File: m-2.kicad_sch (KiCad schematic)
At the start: 12 parts

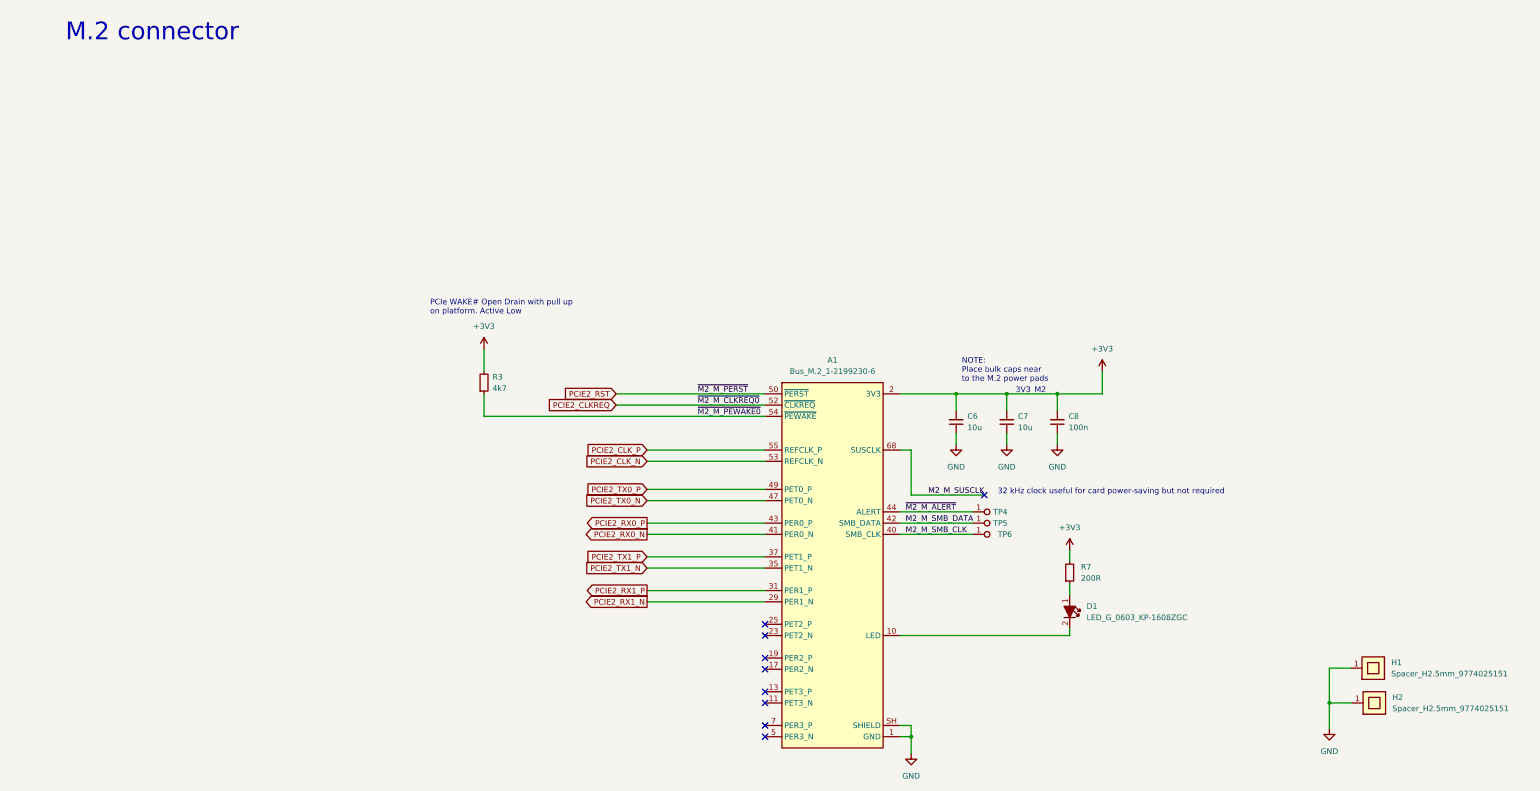
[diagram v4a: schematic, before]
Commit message: [#45990] Fix schematic flaws discussed in review
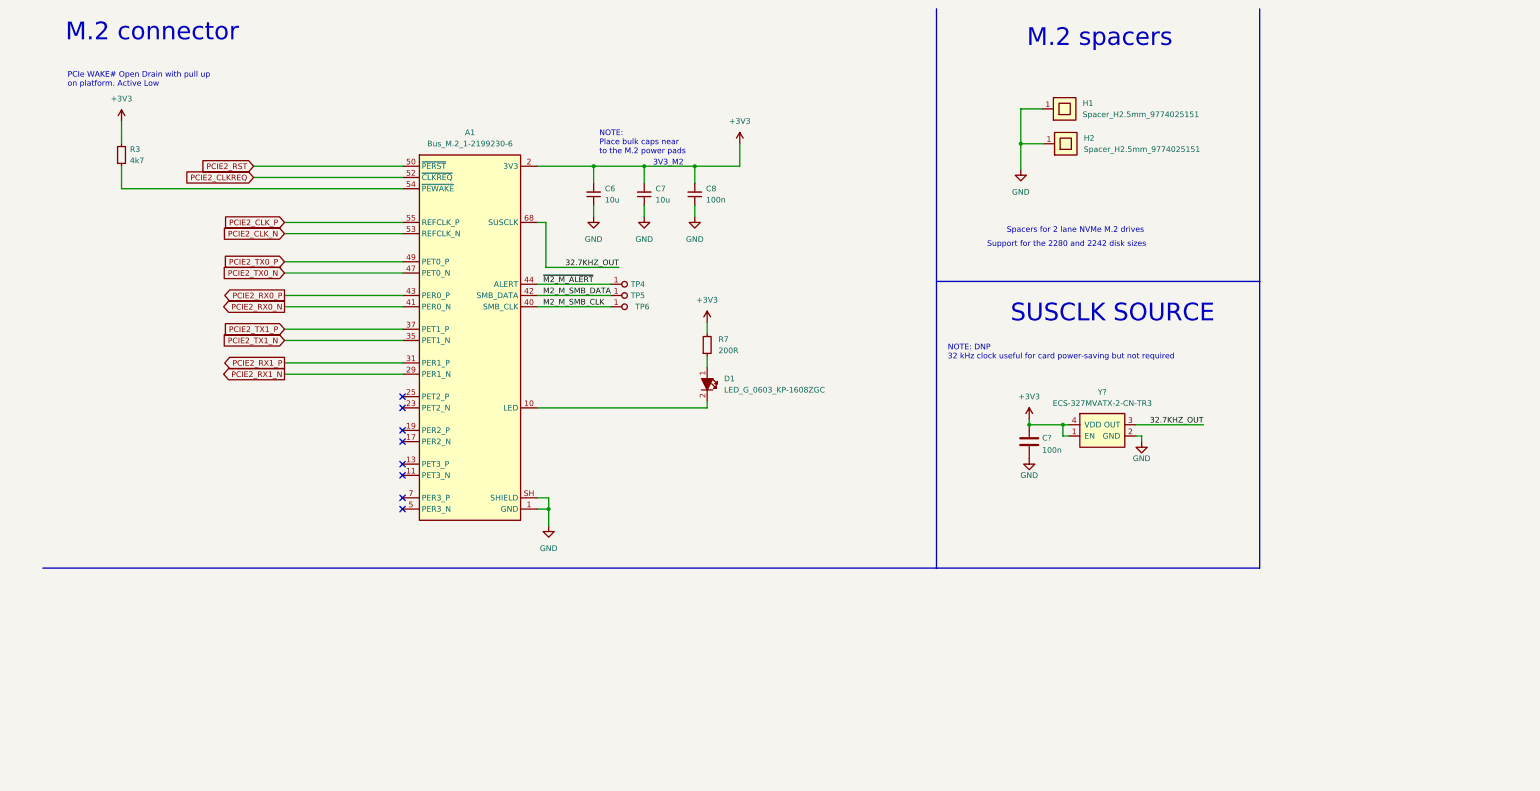
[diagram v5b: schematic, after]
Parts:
- added C?: C_100n_0402, jetson-orin-baseboard-footprints:0402-cap, symbol jetson-orin-baseboard:C_100n_0402
- added Y?: ECS-327MVATX-2-CN-TR3, jetson-orin-baseboard-footprints:Oscillator_SMD_ECS_2520MV-xxx-xx-4Pin_2.5x2.0mm, symbol jetson-orin-baseboard:ECS-327MVATX-2-CN-TR3
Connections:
- net +3V3: now also C?.1, Y?.1 (EN), Y?.4 (VDD)
- net GND: now also C?.2, Y?.2 (GND)
- net M2_M_SUSCLK renamed 32.7KHZ_OUT
- net 32.7KHZ_OUT: now also Y?.3 (OUT)
- net ~{M2_M_PEWAKE0}: no longer names the net of A1.54 (~{PEWAKE}), R3.1
- no-connect marks 9 -> 8
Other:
- note added: "M.2 spacers"
- note added: "NOTE: DNP 32 kHz clock useful for card power-saving but not required"
- note added: "SUSCLK SOURCE"
- note added: "Spacers for 2 lane NVMe M.2 drives"
- note added: "Support for the 2280 and 2242 disk sizes"
- note removed: "32 kHz clock useful for card power-saving but not required"
- moved on the sheet: A1, C6, C7, C8, D1, H1, H2, R3, R7, TP4, TP5, TP6

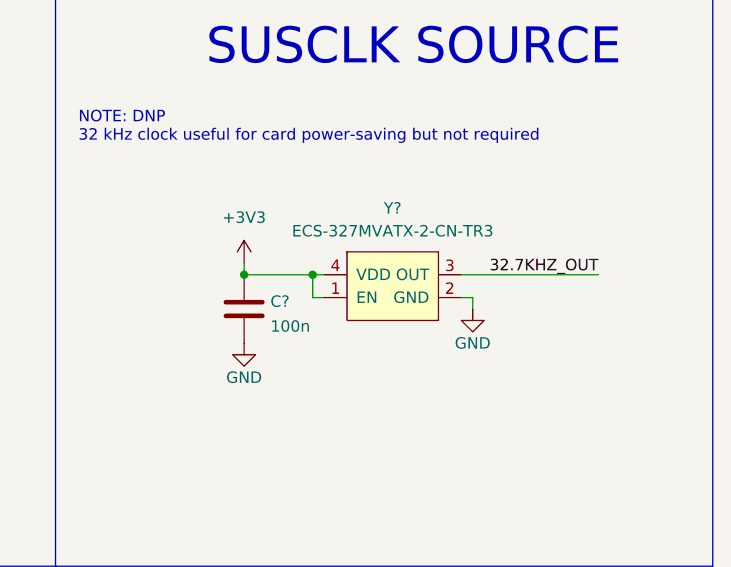
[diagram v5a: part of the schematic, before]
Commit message: [#45990] Route dif Pcie, place susclk gen
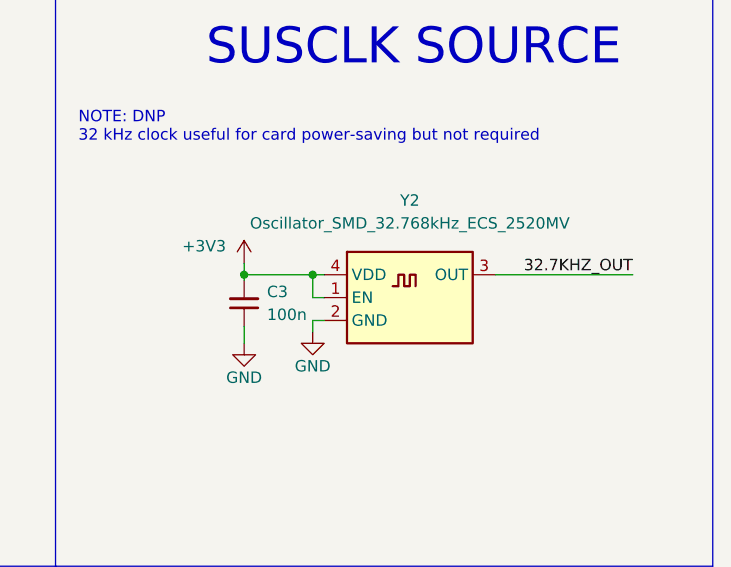
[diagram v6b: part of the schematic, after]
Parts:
- removed C?: C_100n_0402, jetson-orin-baseboard-footprints:0402-cap, symbol jetson-orin-baseboard:C_100n_0402
- removed Y?: ECS-327MVATX-2-CN-TR3, jetson-orin-baseboard-footprints:Oscillator_SMD_ECS_2520MV-xxx-xx-4Pin_2.5x2.0mm, symbol jetson-orin-baseboard:ECS-327MVATX-2-CN-TR3
- added C3: C_100n_0402, antmicro-footprints:C_0402_1005Metric, symbol antmicroCapacitors0402:C_100n_0402
- added Y2: Oscillator_SMD_32.768kHz_ECS_2520MV, antmicro-footprints:Oscillator_SMD_ECS_2520MV_2.5x2mm, symbol antmicroOscillators:Oscillator_SMD_32.768kHz_ECS_2520MV
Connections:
- net +3V3: now also C3.2, Y2.1 (EN), Y2.4 (VDD)
- net 32.7KHZ_OUT: now also Y2.3 (OUT)
- net GND: now also C3.1, Y2.2 (GND)
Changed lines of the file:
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@@
   (no_connect (at 93.345 117.475))
   (no_connect (at 93.345 125.095))
-  (wire (pts (xy 259.08 108.585) (xy 260.35 108.585))
+  (wire (pts (xy 243.84 111.125) (xy 242.57 111.125))
     (stroke (width 0) (type default) (color 0 0 0 0))
   )
@@
     (stroke (width 0) (type default) (color 0 0 0 0))
   )
+  (wire (pts (xy 234.95 111.76) (xy 234.95 113.665))
+    (stroke (width 0) (type default) (color 0 0 0 0))
+  )
   (polyline (pts (xy 287.02 12.065) (xy 287.02 73.66))
     (stroke (width 0) (type default) (color 0 0 0 0))
@@
     (stroke (width 0) (type default) (color 0 0 0 0))
   )
-  (wire (pts (xy 260.35 108.585) (xy 260.35 109.855))
+  (wire (pts (xy 242.57 111.125) (xy 242.57 112.395))
     (stroke (width 0) (type default) (color 0 0 0 0))
   )
@@
     (stroke (width 0) (type default) (color 0 0 0 0))
   )
+  (wire (pts (xy 234.95 106.045) (xy 234.95 106.68))
+    (stroke (width 0) (type default) (color 0 0 0 0))
+  )
   (wire (pts (xy 29.845 52.705) (xy 93.345 52.705))
     (stroke (width 0) (type default) (color 0 0 0 0))
@@
     (stroke (width 0) (type default) (color 0 0 0 0))
   )
-  (wire (pts (xy 274.32 106.045) (xy 259.08 106.045))
+  (wire (pts (xy 278.13 106.045) (xy 262.89 106.045))
     (stroke (width 0) (type default) (color 0 0 0 0))
   )
@@
     (effects (font (size 1.27 1.27)) (justify right bottom))
   )
-  (label "32.7KHZ_OUT" (at 274.32 106.045 180)
+  (label "32.7KHZ_OUT" (at 278.13 106.045 180)
     (effects (font (size 1.27 1.27)) (justify right bottom))
   )
@@
   (symbol (lib_id "jetson-orin-baseboard:GND") (at 234.95 113.665 0) (mirror y) (unit 1)
     (in_bom yes) (on_board yes) (fields_autoplaced)
-    (property "Reference" "#PWR?" (id 0) (at 234.95 120.015 0)
+    (property "Reference" "#PWR0106" (id 0) (at 234.95 120.015 0)
       (effects (font (size 1.27 1.27)) hide)
     )
@@
     (pin "1")
   )
+  (symbol (lib_id "antmicroCapacitors0402:C_100n_0402") (at 234.95 111.76 90) (unit 1)
+    (in_bom yes) (on_board yes) (fields_autoplaced)
+    (property "Reference" "C3" (id 0) (at 237.49 107.9435 90)
+      (effects (font (size 1.27 1.27) (thickness 0.15)) (justify right))
+    )
+    (property "Value" "C_100n_0402" (id 1) (at 245.11 91.44 0)
+      (effects (font (size 1.27 1.27) (thickness 0.15)) (justify left bottom) hide)
+    )
+    (property "Footprint" "antmicro-footprints:C_0402_1005Metric" (id 2) (at 247.65 91.44 0)
+      (effects (font (size 1.27 1.27) (thickness 0.15)) (justify left bottom) hide)
+    )
+    (property "Datasheet" "https://search.murata.co.jp/Ceramy/image/img/A01X/G101/ENG/GRM155R61H104KE14-01.pdf" (id 3) (at 250.19 91.44 0)
+      (effects (font (size 1.27 1.27) (thickness 0.15)) (justify left bottom) hide)
+    )
+    (property "MPN" "GRM155R61H104KE14D" (id 4) (at 252.73 91.44 0)
+      (effects (font (size 1.27 1.27) (thickness 0.15)) (justify left bottom) hide)
+    )
+    (property "Manufacturer" "Murata" (id 5) (at 255.27 91.44 0)
+      (effects (font (size 1.27 1.27) (thickness 0.15)) (justify left bottom) hide)
+    )
+    (property "License" "Apache-2.0" (id 6) (at 257.81 91.44 0)
+      (effects (font (size 1.27 1.27) (thickness 0.15)) (justify left bottom) hide)
+    )
+    (property "Author" "Antmicro" (id 7) (at 260.35 91.44 0)
+      (effects (font (size 1.27 1.27) (thickness 0.15)) (justify left bottom) hide)
+    )
+    (property "Val" "100n" (id 8) (at 237.49 110.4835 90)
+      (effects (font (size 1.27 1.27) (thickness 0.15)) (justify right))
+    )
+    (property "Voltage" "50V" (id 9) (at 262.89 91.44 0)
+      (effects (font (size 1.27 1.27)) (justify left bottom) hide)
+    )
+    (property "Dielectric" "X5R" (id 10) (at 265.43 91.44 0)
+      (effects (font (size 1.27 1.27)) (justify left bottom) hide)
+    )
+    (pin "1")
+    (pin "2")
+  )
   (symbol (lib_id "antmicroResistors0402:R_200R_0402") (at 162.179 90.551 90) (unit 1)
     (in_bom yes) (on_board yes) (fields_autoplaced)
@@
     (pin "2")
   )
+  (symbol (lib_id "antmicroOscillators:Oscillator_SMD_32.768kHz_ECS_2520MV") (at 243.84 106.045 0) (unit 1)
+    (in_bom yes) (on_board yes) (fields_autoplaced)
+    (property "Reference" "Y2" (id 0) (at 253.365 97.79 0)
+      (effects (font (size 1.27 1.27) (thickness 0.15)))
+    )
+    (property "Value" "Oscillator_SMD_32.768kHz_ECS_2520MV" (id 1) (at 253.365 100.33 0)
+      (effects (font (size 1.27 1.27) (thickness 0.15)))
+    )
+    (property "Footprint" "antmicro-footprints:Oscillator_SMD_ECS_2520MV_2.5x2mm" (id 2) (at 295.91 114.935 0)
+      (effects (font (size 1.27 1.27) (thickness 0.15)) (justify left bottom) hide)
+    )
+    (property "Datasheet" "https://eu.mouser.com/datasheet/2/122/ECS_327MVATX-2580060.pdf" (id 3) (at 295.91 117.475 0)
+      (effects (font (size 1.27 1.27) (thickness 0.15)) (justify left bottom) hide)
+    )
+    (property "MPN" "ECS-327MVATX-2-CN-TR3" (id 4) (at 295.91 120.015 0)
+      (effects (font (size 1.27 1.27) (thickness 0.15)) (justify left bottom) hide)
+    )
+    (property "Manufacturer" "ECS Inc." (id 5) (at 295.91 122.555 0)
+      (effects (font (size 1.27 1.27) (thickness 0.15)) (justify left bottom) hide)
+    )
+    (property "VAL" "32.768 kHz" (id 6) (at 295.91 125.095 0)
+      (effects (font (size 1.27 1.27) (thickness 0.15)) (justify left bottom) hide)
+    )
+    (property "Author" "Antmicro" (id 7) (at 295.91 127.635 0)
+      (effects (font (size 1.27 1.27) (thickness 0.15)) (justify left bottom) hide)
+    )
+    (property "License" "Apache-2.0" (id 8) (at 295.91 130.175 0)
+      (effects (font (size 1.27 1.27) (thickness 0.15)) (justify left bottom) hide)
+    )
+    (pin "1")
+    (pin "2")
+    (pin "3")
+    (pin "4")
+  )
   (symbol (lib_id "antmicroCapacitors0402:C_10u_0402") (at 147.955 56.515 90) (unit 1)
     (in_bom yes) (on_board yes) (fields_autoplaced)
@@
     (pin "1")
     (pin "2")
-  )
-  (symbol (lib_id "jetson-orin-baseboard:ECS-327MVATX-2-CN-TR3") (at 251.46 106.045 0) (unit 1)
-    (in_bom yes) (on_board yes) (fields_autoplaced)
-    (property "Reference" "Y?" (id 0) (at 251.46 98.6622 0))
-    (property "Value" "ECS-327MVATX-2-CN-TR3" (id 1) (at 251.46 101.1991 0))
-    (property "Footprint" "jetson-orin-baseboard-footprints:Oscillator_SMD_ECS_2520MV-xxx-xx-4Pin_2.5x2.0mm" (id 2) (at 250.19 113.665 0)
-      (effects (font (size 1.27 1.27)) hide)
-    )
-    (property "Datasheet" "https://eu.mouser.com/datasheet/2/122/ECS_327MVATX-2580060.pdf" (id 3) (at 254 93.345 0)
-      (effects (font (size 1.27 1.27)) hide)
-    )
-    (property "MPN" "ECS-327MVATX-2-CN-TR3" (id 4) (at 252.73 98.425 0)
-      (effects (font (size 1.27 1.27)) hide)
-    )
-    (property "Manufacturer" "ECS" (id 5) (at 251.46 95.885 0)
-      (effects (font (size 1.27 1.27)) hide)
-    )
-    (pin "1")
-    (pin "2")
-    (pin "3")
-    (pin "4")
   )
   (symbol (lib_id "antmicroTestPoints:TP_0.75mm_SMD") (at 140.335 76.835 0) (unit 1)
@@
   )
   (symbol (lib_id "jetson-orin-baseboard:+3V3") (at 234.95 104.775 0) (unit 1)
-    (in_bom yes) (on_board yes) (fields_autoplaced)
-    (property "Reference" "#PWR?" (id 0) (at 234.95 108.585 0)
+    (in_bom yes) (on_board yes)
+    (property "Reference" "#PWR0107" (id 0) (at 234.95 108.585 0)
       (effects (font (size 1.27 1.27)) hide)
     )
-    (property "Value" "+3V3" (id 1) (at 234.95 99.695 0))
+    (property "Value" "+3V3" (id 1) (at 230.505 102.87 0))
     (property "Footprint" "" (id 2) (at 234.95 104.775 0)
       (effects (font (size 1.27 1.27)) hide)
@@
     (pin "2")
   )
-  (symbol (lib_id "jetson-orin-baseboard:GND") (at 260.35 109.855 0) (mirror y) (unit 1)
+  (symbol (lib_id "jetson-orin-baseboard:GND") (at 242.57 112.395 0) (unit 1)
     (in_bom yes) (on_board yes) (fields_autoplaced)
-    (property "Reference" "#PWR?" (id 0) (at 260.35 116.205 0)
+    (property "Reference" "#PWR0104" (id 0) (at 242.57 118.745 0)
       (effects (font (size 1.27 1.27)) hide)
     )
-    (property "Value" "GND" (id 1) (at 260.35 113.665 0))
-    (property "Footprint" "" (id 2) (at 260.35 109.855 0)
+    (property "Value" "GND" (id 1) (at 242.57 116.205 0))
+    (property "Footprint" "" (id 2) (at 242.57 112.395 0)
       (effects (font (size 1.27 1.27)) hide)
     )
-    (property "Datasheet" "" (id 3) (at 260.35 109.855 0)
+    (property "Datasheet" "" (id 3) (at 242.57 112.395 0)
       (effects (font (size 1.27 1.27)) hide)
     )
     (pin "1")
   )
-  (symbol (lib_id "jetson-orin-baseboard:C_100n_0402") (at 234.95 109.855 0) (unit 1)
-    (in_bom yes) (on_board yes) (fields_autoplaced)
-    (property "Reference" "C?" (id 0) (at 237.871 109.0204 0)
-      (effects (font (size 1.27 1.27)) (justify left))
-    )
-    (property "Value" "C_100n_0402" (id 1) (at 234.95 113.665 0)
-      (effects (font (size 1.27 1.27)) hide)
-    )
-    (property "Footprint" "jetson-orin-baseboard-footprints:0402-cap" (id 2) (at 240.03 104.775 0)
-      (effects (font (size 1.524 1.524)) (justify left) hide)
-    )
-    (property "Datasheet" "" (id 3) (at 234.95 109.855 0)
-      (effects (font (size 1.27 1.27)) hide)
-    )
-    (property "Manufacturer" "Murata" (id 4) (at 240.03 99.695 0)
-      (effects (font (size 1.524 1.524)) (justify left) hide)
-    )
-    (property "MPN" "GRM155R61H104KE14D" (id 5) (at 240.03 102.235 0)
-      (effects (font (size 1.524 1.524)) (justify left) hide)
-    )
-    (property "Val" "100n" (id 6) (at 237.871 111.7855 0)
-      (effects (font (size 1.27 1.27)) (justify left))
-    )
-    (pin "1")
-    (pin "2")
-  )
   (symbol (lib_id "antmicropower:+3V3") (at 29.845 37.465 0) (unit 1)
